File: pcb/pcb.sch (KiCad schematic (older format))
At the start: 32 parts, among them J1 BAT+, J10 GRN, J11 RED, J12 Load Cell, J2 BAT-, J3 Battery, J4 DS18B20, J5 TMP+, J6 TMPO, J7 TMP-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

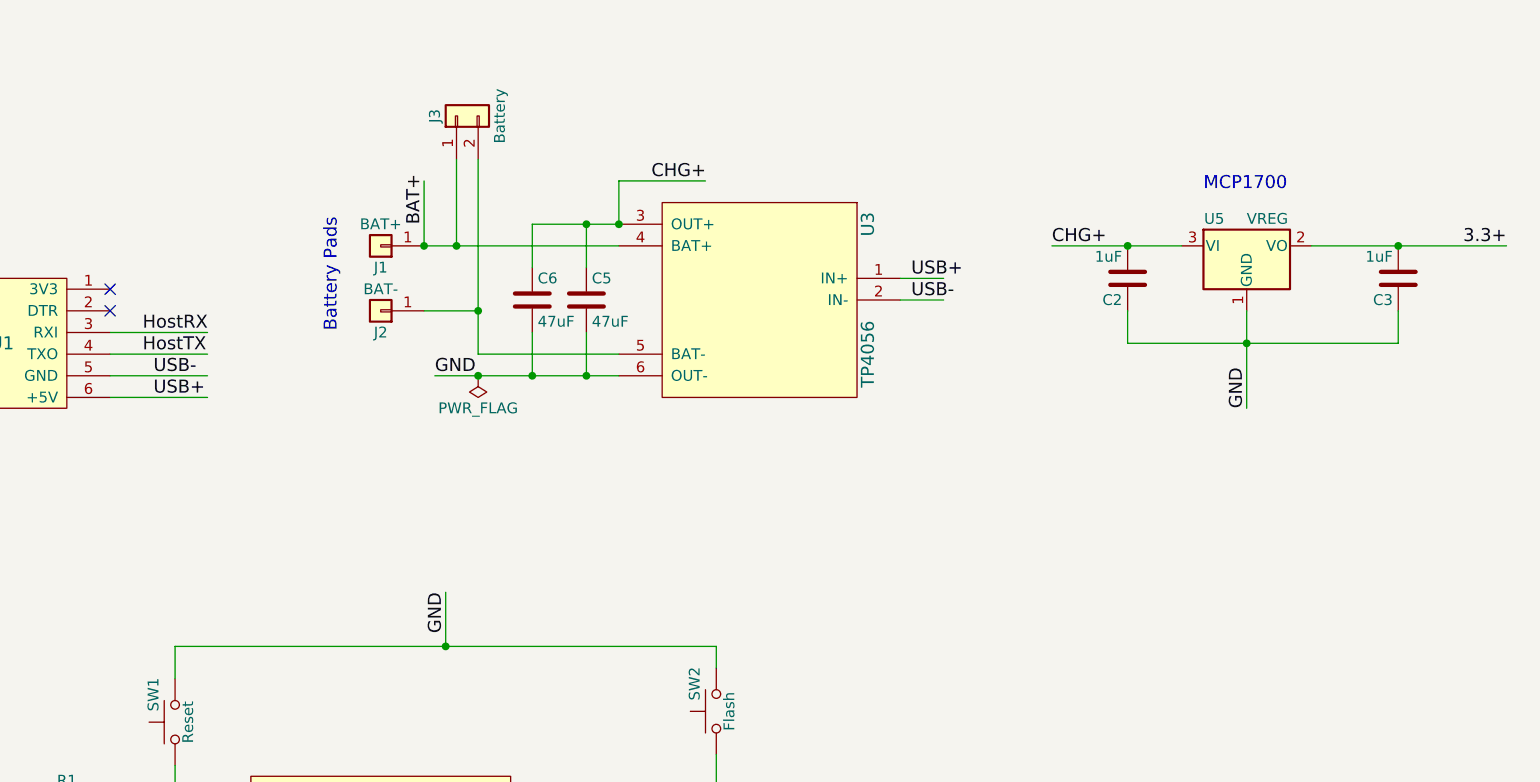
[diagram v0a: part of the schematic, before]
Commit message: Another crack at a battery disconnector circuit
I found an example on the Arduino forums (link at end). It uses a
p-channel MOSFET 'backwards', with source connected to the load
and drain to the battery. The parasitic diode therefore blocks
leakage back into the battery. USB is connected to the gate and also
to the load, the latter via Schottky diode, to prevent battery
voltage from sneaking back through the circuit to flip the MOSFET.

A large capacitor buffers between the voltage regulator and ground,
to ensure that the system doesn't lose power while things are switching.
(The MOSFET takes on the order of nanoseconds to switch; the 47uF
capacitor between VREG+ and GND can run the ESP at peak current for
about 15 milliseconds, and the ESP has its own 47uF capacitor, too.)

You can see the circuit in action here: https://www.systemvision.com/design/pendulum-pcb-battery-disconnector/

Forum thread here: http://forum.arduino.cc/index.php?topic=496727.0
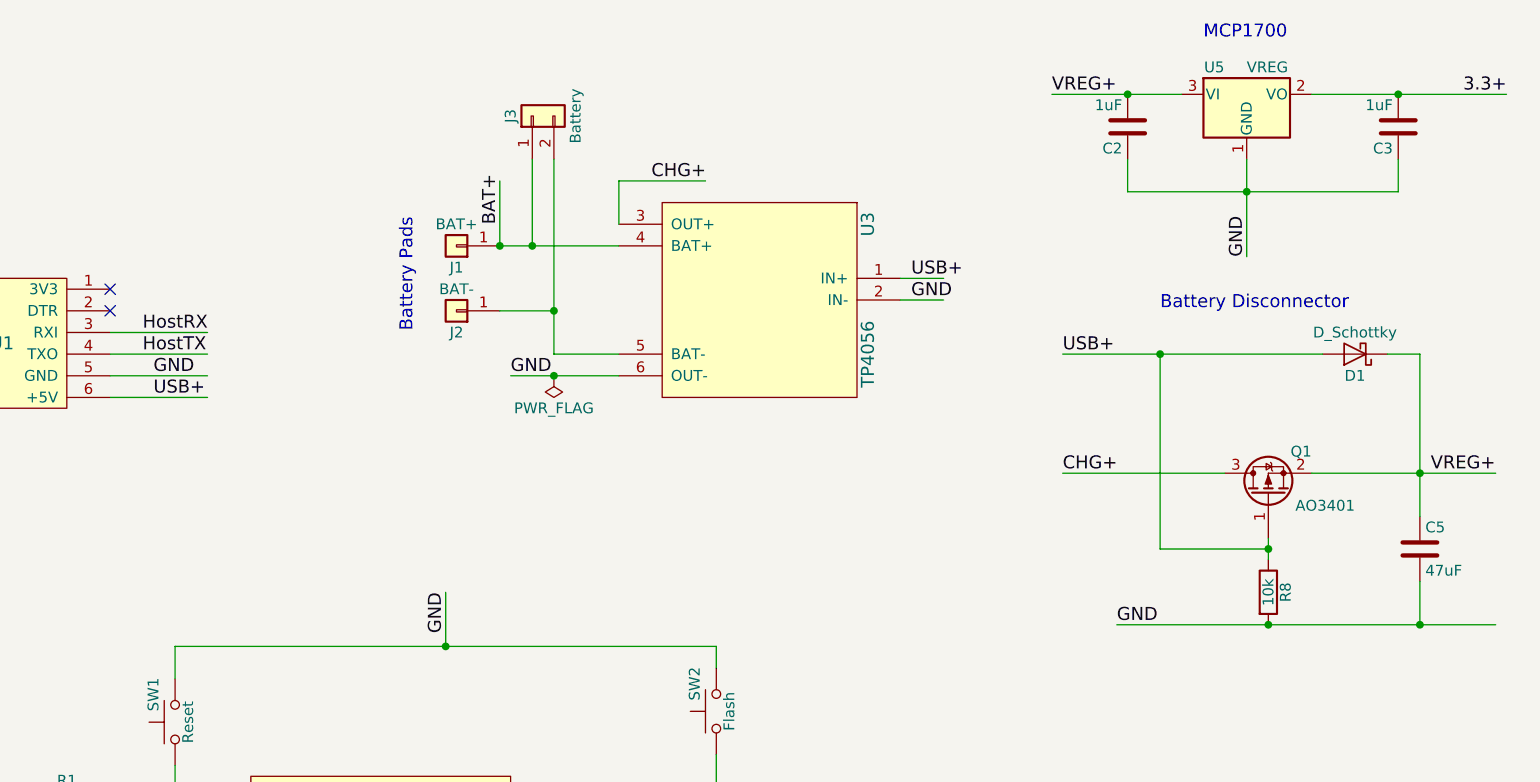
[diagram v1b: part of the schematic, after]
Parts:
- removed C6: 47uF, Capacitors_SMD:C_0805, symbol C
- added D1: D_Schottky, Diodes_SMD:D_0805, symbol D_Schottky
- added Q1: AO3401, TO_SOT_Packages_SMD:SOT-23, symbol NTR2101P
- added R8: 10k, Resistors_SMD:R_0805, symbol R
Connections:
- net labels added: VREG+
- net labels removed: USB-
- wire segments 87 -> 92
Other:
- note added: "Battery Disconnector"
- moved on the sheet: C2, C3, J1, J2, J3, U5
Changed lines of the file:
@@
 L MCP1700-3302E_SOT23 U5
 U 1 1 5B217881
-P 8850 2250
-F 0 "U5" H 8700 2375 50  0000 C CNN
-F 1 "VREG" H 8850 2375 50  0000 L CNN
-F 2 "TO_SOT_Packages_SMD:SOT-23" H 8850 2475 50  0001 C CNN
-F 3 "" H 8850 2250 50  0001 C CNN
-	1    8850 2250
+P 8850 1550
+F 0 "U5" H 8700 1675 50  0000 C CNN
+F 1 "VREG" H 8850 1675 50  0000 L CNN
+F 2 "TO_SOT_Packages_SMD:SOT-23" H 8850 1775 50  0001 C CNN
+F 3 "" H 8850 1550 50  0001 C CNN
+	1    8850 1550
 	1    0    0    -1
 $EndComp
@@
 L Conn_01x01 J1
 U 1 1 5B217852
-P 4850 2250
-F 0 "J1" H 4850 2350 50  0000 C CNN
-F 1 "BAT+" H 4850 2150 50  0000 C CNN
-F 2 "Extra_Pads:SolderWirePad_single_SMD_5x3mm" H 4850 2250 50  0001 C CNN
-F 3 "" H 4850 2250 50  0001 C CNN
-	1    4850 2250
+P 5200 2250
+F 0 "J1" H 5200 2350 50  0000 C CNN
+F 1 "BAT+" H 5200 2150 50  0000 C CNN
+F 2 "Extra_Pads:SolderWirePad_single_SMD_5x3mm" H 5200 2250 50  0001 C CNN
+F 3 "" H 5200 2250 50  0001 C CNN
+	1    5200 2250
 	-1   0    0    1
 $EndComp
@@
 L Conn_01x01 J2
 U 1 1 5B2178B3
-P 4850 2550
-F 0 "J2" H 4850 2650 50  0000 C CNN
-F 1 "BAT-" H 4850 2450 50  0000 C CNN
-F 2 "Extra_Pads:SolderWirePad_single_SMD_5x3mm" H 4850 2550 50  0001 C CNN
-F 3 "" H 4850 2550 50  0001 C CNN
-	1    4850 2550
+P 5200 2550
+F 0 "J2" H 5200 2650 50  0000 C CNN
+F 1 "BAT-" H 5200 2450 50  0000 C CNN
+F 2 "Extra_Pads:SolderWirePad_single_SMD_5x3mm" H 5200 2550 50  0001 C CNN
+F 3 "" H 5200 2550 50  0001 C CNN
+	1    5200 2550
 	-1   0    0    1
 $EndComp
@@
 USB+
 Text Label 7300 2500 0    60   ~ 0
-USB-
+GND
 Text Label 6100 1950 0    60   ~ 0
 CHG+
-Text Label 9850 2250 0    60   ~ 0
+Text Label 9850 1550 0    60   ~ 0
 3.3+
-Text Label 8850 3000 1    60   ~ 0
-GND
-Text Label 5050 2150 1    60   ~ 0
+Text Label 8850 2300 1    60   ~ 0
+GND
+Text Label 5400 2150 1    60   ~ 0
 BAT+
 Text Label 3800 2850 0    60   ~ 0
-USB-
+GND
 Text Label 1950 4250 0    60   ~ 0
 BAT+
@@
 L C C3
 U 1 1 5B2296F3
-P 9550 2400
-F 0 "C3" H 9575 2500 50  0000 L CNN
-F 1 "1uF" H 9575 2300 50  0000 L CNN
-F 2 "Capacitors_SMD:C_0805" H 9588 2250 50  0001 C CNN
-F 3 "" H 9550 2400 50  0001 C CNN
-	1    9550 2400
+P 9550 1700
+F 0 "C3" H 9575 1800 50  0000 L CNN
+F 1 "1uF" H 9575 1600 50  0000 L CNN
+F 2 "Capacitors_SMD:C_0805" H 9588 1550 50  0001 C CNN
+F 3 "" H 9550 1700 50  0001 C CNN
+	1    9550 1700
 	-1   0    0    1
 $EndComp
@@
 NoConn ~ 3600 2450
 NoConn ~ 3600 2550
-Text Notes 4750 2650 1    60   ~ 0
+Text Notes 5100 2650 1    60   ~ 0
 Battery Pads\n\n
 $Comp
 L Conn_01x02 J3
 U 1 1 5B22789F
-P 5200 1650
-F 0 "J3" H 5200 1750 50  0000 C CNN
-F 1 "Battery" H 5200 1450 50  0000 C CNN
-F 2 "Connectors_Molex:Molex_PicoBlade_53048-0210_02x1.25mm_Angled" H 5200 1650 50  0001 C CNN
-F 3 "" H 5200 1650 50  0001 C CNN
-	1    5200 1650
-	0    -1   -1   0
-$EndComp
-Text Notes 8650 2000 0    60   ~ 0
+P 5550 1650
+F 0 "J3" H 5550 1750 50  0000 C CNN
+F 1 "Battery" H 5550 1450 50  0000 C CNN
+F 2 "Connectors_Molex:Molex_PicoBlade_53048-0210_02x1.25mm_Angled" H 5550 1650 50  0001 C CNN
+F 3 "" H 5550 1650 50  0001 C CNN
+	1    5550 1650
+	0    -1   -1   0
+$EndComp
+Text Notes 8650 1300 0    60   ~ 0
 MCP1700
 $Comp
@@
 L C C2
 U 1 1 5B241212
-P 8300 2400
-F 0 "C2" H 8325 2500 50  0000 L CNN
-F 1 "1uF" H 8325 2300 50  0000 L CNN
-F 2 "Capacitors_SMD:C_0805" H 8338 2250 50  0001 C CNN
-F 3 "" H 8300 2400 50  0001 C CNN
-	1    8300 2400
+P 8300 1700
+F 0 "C2" H 8325 1800 50  0000 L CNN
+F 1 "1uF" H 8325 1600 50  0000 L CNN
+F 2 "Capacitors_SMD:C_0805" H 8338 1550 50  0001 C CNN
+F 3 "" H 8300 1700 50  0001 C CNN
+	1    8300 1700
 	-1   0    0    1
 $EndComp
@@
 	5950 1950 6350 1950
 Wire Wire Line
-	8850 2550 8850 3000
-Wire Wire Line
-	9150 2250 10050 2250
-Wire Wire Line
-	5050 2250 5950 2250
+	8850 1850 8850 2300
+Wire Wire Line
+	9150 1550 10050 1550
 Wire Wire Line
 	5750 5000 6150 5000
@@
 	3650 5000 3950 5000
 Wire Wire Line
-	5050 2250 5050 1950
-Connection ~ 5050 2250
-Wire Wire Line
-	5050 2550 5300 2550
-Wire Wire Line
-	5200 1850 5200 2250
-Connection ~ 5200 2250
-Wire Wire Line
-	5300 1850 5300 2750
-Connection ~ 5300 2550
+	5400 2250 5400 1950
+Connection ~ 5400 2250
+Wire Wire Line
+	5400 2550 5650 2550
+Wire Wire Line
+	5550 1850 5550 2250
+Connection ~ 5550 2250
+Wire Wire Line
+	5650 1850 5650 2750
+Connection ~ 5650 2550
 Wire Wire Line
 	3850 5700 3850 6500
@@
 	6000 6500 5000 6500
 Wire Wire Line
-	9550 2700 9550 2550
-Wire Wire Line
-	8300 2700 9550 2700
-Connection ~ 9550 2250
-Wire Wire Line
-	8300 2550 8300 2700
+	9550 2000 9550 1850
+Wire Wire Line
+	8300 2000 9550 2000
+Connection ~ 9550 1550
+Wire Wire Line
+	8300 1850 8300 2000
 Wire Wire Line
 	6000 6500 6000 5700
@@
 	6450 5600 6450 5700
 Connection ~ 6450 5700
-Connection ~ 8850 2700
+Connection ~ 8850 2000
 Wire Wire Line
 	3600 2750 4050 2750
@@
 L PWR_FLAG #FLG03
 U 1 1 5B2F14F2
-P 5300 2850
-F 0 "#FLG03" H 5300 2925 50  0001 C CNN
-F 1 "PWR_FLAG" H 5300 3000 50  0000 C CNN
-F 2 "" H 5300 2850 50  0001 C CNN
-F 3 "" H 5300 2850 50  0001 C CNN
-	1    5300 2850
-	-1   0    0    1
-$EndComp
-Connection ~ 5300 2850
-Connection ~ 8300 2250
+P 5650 2850
+F 0 "#FLG03" H 5650 2925 50  0001 C CNN
+F 1 "PWR_FLAG" H 5650 3000 50  0000 C CNN
+F 2 "" H 5650 2850 50  0001 C CNN
+F 3 "" H 5650 2850 50  0001 C CNN
+	1    5650 2850
+	-1   0    0    1
+$EndComp
+Connection ~ 5650 2850
+Connection ~ 8300 1550
 Wire Wire Line
 	3600 2850 4050 2850
 Wire Wire Line
-	5100 2850 5950 2850
+	7950 1550 8550 1550
+Text Label 7950 1550 0    60   ~ 0
+VREG+
+Text Label 5450 2850 0    60   ~ 0
+GND
+Wire Wire Line
+	5950 2250 5400 2250
+Wire Wire Line
+	5650 2750 5950 2750
+Wire Wire Line
+	5450 2850 5950 2850
+$Comp
+L D_Schottky D1
+U 1 1 5B303989
+P 9350 2750
+F 0 "D1" H 9350 2850 50  0000 C CNN
+F 1 "D_Schottky" H 9350 2650 50  0000 C CNN
+F 2 "Diodes_SMD:D_0805" H 9350 2750 50  0001 C CNN
+F 3 "" H 9350 2750 50  0001 C CNN
+	1    9350 2750
+	-1   0    0    1
+$EndComp
+$Comp
+L NTR2101P Q1
+U 1 1 5B303A3D
+P 8950 3400
+F 0 "Q1" V 9150 3200 50  0000 L CNN
+F 1 "AO3401" V 8900 3000 50  0000 L CNN
+F 2 "TO_SOT_Packages_SMD:SOT-23" H 9150 3325 50  0001 L CIN
+F 3 "" H 8950 3400 50  0001 L CNN
+	1    8950 3400
+	0    -1   -1   0
+$EndComp
+$Comp
+L R R8
+U 1 1 5B304CC6
+P 8950 3850
+F 0 "R8" V 9030 3850 50  0000 C CNN
+F 1 "10k" V 8950 3850 50  0000 C CNN
+F 2 "Resistors_SMD:R_0805" V 8880 3850 50  0001 C CNN
+F 3 "" H 8950 3850 50  0001 C CNN
+	1    8950 3850
+	1    0    0    -1
+$EndComp
+Wire Wire Line
+	8000 2750 9200 2750
+Wire Wire Line
+	9500 2750 9650 2750
+Wire Wire Line
+	9650 2750 9650 3500
+Wire Wire Line
+	9150 3300 10000 3300
+Connection ~ 9650 3300
+Text Label 9700 3300 0    60   ~ 0
+VREG+
+Text Label 8000 2750 0    60   ~ 0
+USB+
+Wire Wire Line
+	8950 3600 8950 3700
+Connection ~ 8950 3650
+Wire Wire Line
+	8250 4000 10000 4000
+Connection ~ 8950 4000
+Text Label 8250 4000 0    60   ~ 0
+GND
+Wire Wire Line
+	8000 3300 8750 3300
+Text Label 8000 3300 0    60   ~ 0
+CHG+
+Wire Wire Line
+	8450 2750 8450 3650
+Wire Wire Line
+	8450 3650 8950 3650
+Connection ~ 8450 2750
+Text Notes 8450 2550 0    60   ~ 0
+Battery Disconnector
 $Comp
 L C C5
-U 1 1 5B301162
-P 5800 2500
-F 0 "C5" H 5825 2600 50  0000 L CNN
-F 1 "47uF" H 5825 2400 50  0000 L CNN
-F 2 "Capacitors_SMD:C_0805" H 5838 2350 50  0001 C CNN
-F 3 "" H 5800 2500 50  0001 C CNN
-	1    5800 2500
+U 1 1 5B308A6C
+P 9650 3650
+F 0 "C5" H 9675 3750 50  0000 L CNN
+F 1 "47uF" H 9675 3550 50  0000 L CNN
+F 2 "Capacitors_SMD:C_0805" H 9688 3500 50  0001 C CNN
+F 3 "" H 9650 3650 50  0001 C CNN
+	1    9650 3650
 	1    0    0    -1
 $EndComp
 Wire Wire Line
-	5300 2750 5950 2750
-Wire Wire Line
-	5550 2150 5950 2150
-Wire Wire Line
-	5800 2150 5800 2350
-Wire Wire Line
-	5800 2850 5800 2650
-Connection ~ 5800 2850
-Connection ~ 5950 2150
-Wire Wire Line
-	7950 2250 8550 2250
-Text Label 7950 2250 0    60   ~ 0
-CHG+
-Text Label 5100 2850 0    60   ~ 0
-GND
-$Comp
-L C C6
-U 1 1 5B3032B2
-P 5550 2500
-F 0 "C6" H 5575 2600 50  0000 L CNN
-F 1 "47uF" H 5575 2400 50  0000 L CNN
-F 2 "Capacitors_SMD:C_0805" H 5588 2350 50  0001 C CNN
-F 3 "" H 5550 2500 50  0001 C CNN
-	1    5550 2500
-	1    0    0    -1
-$EndComp
-Wire Wire Line
-	5550 2150 5550 2350
-Connection ~ 5800 2150
-Wire Wire Line
-	5550 2650 5550 2850
-Connection ~ 5550 2850
+	9650 3800 9650 4000
+Connection ~ 9650 4000
 $EndSCHEMATC

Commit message: Switch to 1206 footprint for Schottky diode; 0805 seems hard to find
At least at the rated power we need (up to about 500ma).
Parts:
- D1: footprint Diodes_SMD:D_0805 -> Diodes_SMD:D_1206
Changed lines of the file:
@@
 F 0 "D1" H 9350 2850 50  0000 C CNN
 F 1 "D_Schottky" H 9350 2650 50  0000 C CNN
-F 2 "Diodes_SMD:D_0805" H 9350 2750 50  0001 C CNN
+F 2 "Diodes_SMD:D_1206" H 9350 2750 50  0001 C CNN
 F 3 "" H 9350 2750 50  0001 C CNN
 	1    9350 2750

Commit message: Use correct diode SMD package (DO-214AC/SMA)
That's the package all the high-power ones seem to come in.
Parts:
- D1: footprint Diodes_SMD:D_1206 -> Diodes_SMD:D_SMA
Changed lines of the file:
@@
 F 0 "D1" H 9350 2850 50  0000 C CNN
 F 1 "D_Schottky" H 9350 2650 50  0000 C CNN
-F 2 "Diodes_SMD:D_1206" H 9350 2750 50  0001 C CNN
+F 2 "Diodes_SMD:D_SMA" H 9350 2750 50  0001 C CNN
 F 3 "" H 9350 2750 50  0001 C CNN
 	1    9350 2750

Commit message: pcb-1.0.0-rc.4
Just a few final tweaks—labeling, adding a capacitor across USB
in for filtering.
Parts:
- added C6: 1uF, Capacitors_SMD:C_0805, symbol C
- renumbered U1 to CN1, U3 to CN2, U4 to CN3, U5 to U1
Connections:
- wire segments 92 -> 96
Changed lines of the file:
@@
 Sheet 1 1
 Title "Pendulum PCB"
-Date "2018-06-24"
-Rev "1.0.0-rc.3"
+Date "2018-06-25"
+Rev "1.0.0-rc.4"
 Comp ""
 Comment1 ""
@@
 $EndComp
 $Comp
-L MCP1700-3302E_SOT23 U5
+L MCP1700-3302E_SOT23 U1
 U 1 1 5B217881
 P 8850 1550
-F 0 "U5" H 8700 1675 50  0000 C CNN
+F 0 "U1" H 8700 1675 50  0000 C CNN
 F 1 "VREG" H 8850 1675 50  0000 L CNN
 F 2 "TO_SOT_Packages_SMD:SOT-23" H 8850 1775 50  0001 C CNN
@@
 $EndComp
 $Comp
-L TP4056 U3
+L TP4056 CN2
 U 1 1 5B217C78
 P 6150 2950
-F 0 "U3" H 5350 3900 60  0000 C CNN
+F 0 "CN2" H 5350 3900 60  0000 C CNN
 F 1 "TP4056" H 5950 3900 60  0000 C CNN
 F 2 "TP4056:TP4056" H 5300 3900 60  0001 C CNN
@@
 	0    1    1    0
 $EndComp
-Text Label 3800 2950 0    60   ~ 0
+Text Label 3800 3250 0    60   ~ 0
 USB+
 Text Label 3750 2750 0    60   ~ 0
@@
 $EndComp
 $Comp
-L CP2102-BREAKOUT U1
+L CP2102-BREAKOUT CN1
 U 1 1 5B258589
 P 2950 2400
-F 0 "U1" H 3100 2100 60  0000 C CNN
+F 0 "CN1" H 3100 2100 60  0000 C CNN
 F 1 "CP2102-BREAKOUT" V 2900 2100 60  0000 C CNN
 F 2 "CP2102-BRK:CP2102-BREAKOUT" H 2950 2400 60  0001 C CNN
@@
 $EndComp
 $Comp
-L HX711_BREAKOUT U4
+L HX711_BREAKOUT CN3
 U 1 1 5B293345
 P 8650 5850
-F 0 "U4" H 9150 5250 60  0000 C CNN
+F 0 "CN3" H 9150 5250 60  0000 C CNN
 F 1 "HX711_BREAKOUT" H 9150 5900 60  0000 C CNN
 F 2 "HX711-XNQ:HX711-MINI" H 8650 5850 60  0001 C CNN
@@
 Wire Wire Line
 	3600 2650 4050 2650
-Wire Wire Line
-	3600 2950 4050 2950
 Wire Wire Line
 	7650 5450 7300 5450
@@
 	1150 4250 2150 4250
 Connection ~ 1200 6400
-$Comp
-L PWR_FLAG #FLG03
-U 1 1 5B2F14F2
-P 5650 2850
-F 0 "#FLG03" H 5650 2925 50  0001 C CNN
-F 1 "PWR_FLAG" H 5650 3000 50  0000 C CNN
-F 2 "" H 5650 2850 50  0001 C CNN
-F 3 "" H 5650 2850 50  0001 C CNN
-	1    5650 2850
-	-1   0    0    1
-$EndComp
-Connection ~ 5650 2850
 Connection ~ 8300 1550
 Wire Wire Line
@@
 	9650 3800 9650 4000
 Connection ~ 9650 4000
+$Comp
+L C C6
+U 1 1 5B319707
+P 3700 3050
+F 0 "C6" H 3725 3150 50  0000 L CNN
+F 1 "1uF" H 3800 3050 50  0000 L CNN
+F 2 "Capacitors_SMD:C_0805" H 3738 2900 50  0001 C CNN
+F 3 "" H 3700 3050 50  0001 C CNN
+	1    3700 3050
+	1    0    0    -1
+$EndComp
+Wire Wire Line
+	3600 3250 4050 3250
+Wire Wire Line
+	3600 2950 3600 3250
+Connection ~ 3700 3250
+Wire Wire Line
+	3700 3200 3700 3250
+Wire Wire Line
+	3700 2900 3700 2850
+Connection ~ 3700 2850
+$Comp
+L PWR_FLAG #FLG03
+U 1 1 5B3226ED
+P 9950 3400
+F 0 "#FLG03" H 9950 3475 50  0001 C CNN
+F 1 "PWR_FLAG" H 9700 3400 50  0000 C CNN
+F 2 "" H 9950 3400 50  0001 C CNN
+F 3 "" H 9950 3400 50  0001 C CNN
+	1    9950 3400
+	-1   0    0    1
+$EndComp
+Wire Wire Line
+	9950 3400 9950 3300
+Connection ~ 9950 3300
 $EndSCHEMATC

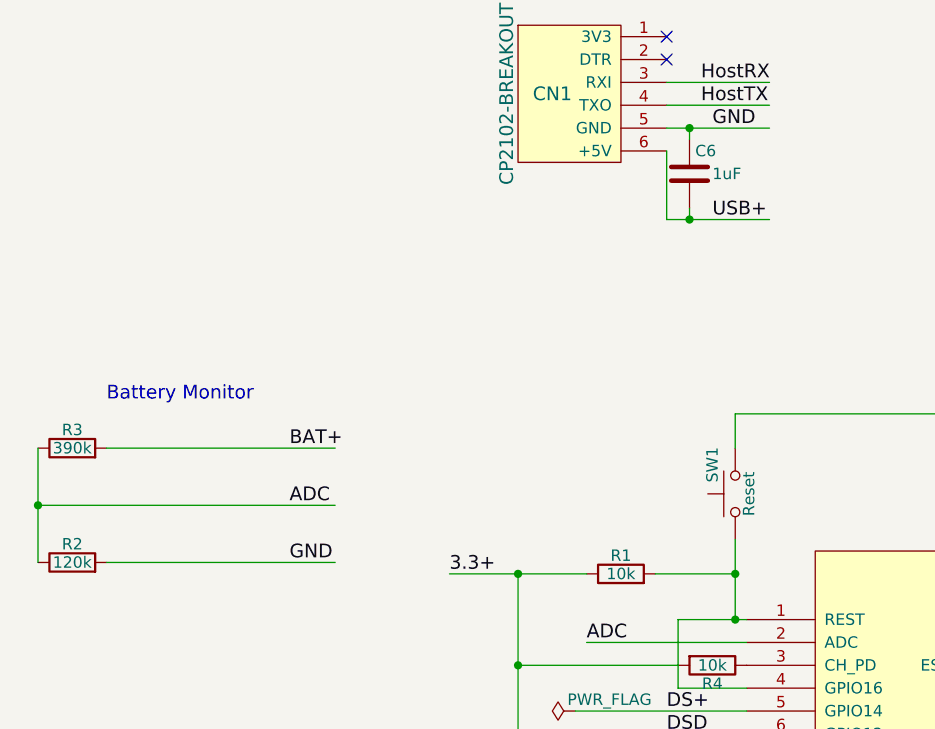
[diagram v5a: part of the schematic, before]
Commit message: More capacitance! More ground pour!
Per recommendations. The ADC trace is long and very low-current,
and needs some smoothing for EMI reasons. The ground pour is bigger
to reduce the number of long traces to ground.
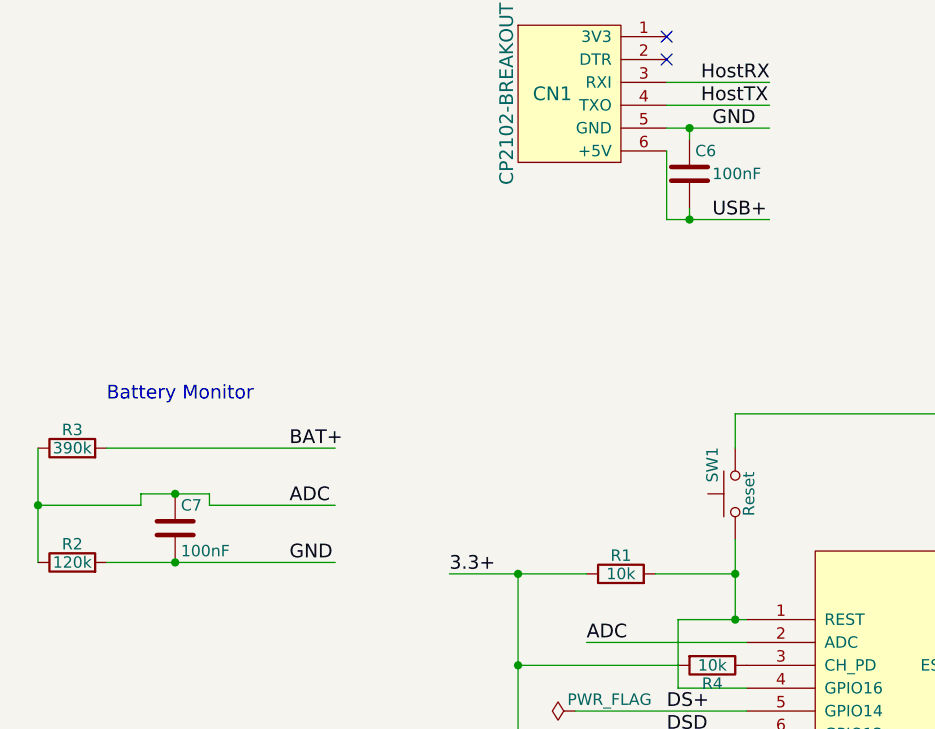
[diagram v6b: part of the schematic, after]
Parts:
- added C7: 100nF, Capacitors_SMD:C_0805, symbol C
- C6: value 1uF -> 100nF
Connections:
- wire segments 96 -> 100
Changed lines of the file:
@@
 	3950 5100 3250 5100
-Wire Wire Line
-	850  4500 2150 4500
 Wire Wire Line
 	3600 5500 3950 5500
@@
 P 3700 3050
 F 0 "C6" H 3725 3150 50  0000 L CNN
-F 1 "1uF" H 3800 3050 50  0000 L CNN
+F 1 "100nF" H 3800 3050 50  0000 L CNN
 F 2 "Capacitors_SMD:C_0805" H 3738 2900 50  0001 C CNN
 F 3 "" H 3700 3050 50  0001 C CNN
@@
 	9950 3400 9950 3300
 Connection ~ 9950 3300
+$Comp
+L C C7
+U 1 1 5B31BCB8
+P 1450 4600
+F 0 "C7" H 1475 4700 50  0000 L CNN
+F 1 "100nF" H 1475 4500 50  0000 L CNN
+F 2 "Capacitors_SMD:C_0805" H 1488 4450 50  0001 C CNN
+F 3 "" H 1450 4600 50  0001 C CNN
+	1    1450 4600
+	1    0    0    -1
+$EndComp
+Wire Wire Line
+	850  4500 1300 4500
+Wire Wire Line
+	1600 4500 2150 4500
+Wire Wire Line
+	1300 4500 1300 4450
+Wire Wire Line
+	1300 4450 1600 4450
+Wire Wire Line
+	1600 4450 1600 4500
+Connection ~ 1450 4450
+Connection ~ 1450 4750
 $EndSCHEMATC

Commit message: pcb-1.0.0-rc.5, blog post
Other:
- moved on the sheet: C2, C3, C5, C6, CN1, CN2, D1, J1, J2, J3, Q1, R8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
